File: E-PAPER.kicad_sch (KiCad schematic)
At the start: 33 parts, among them J6 Conn_01x34_Female, J7 Conn_01x40_Female, U10 TPS65185RGZR

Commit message: Update (Display)
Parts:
- removed C83: 4µ7, Capacitor_SMD:C_0805_2012Metric, symbol Device:C
- removed R50: R, symbol Device:R
- added C85: 22µ, Capacitor_SMD:C_0603_1608Metric, symbol Device:C
- added R54: 1MEG, symbol Device:R
- C84: value C -> 22µ; footprint (none) -> Capacitor_SMD:C_0603_1608Metric; LCSC (none) -> C2762594
- L4: value 4µ7 -> 2µ2; footprint (none) -> Inductor_SMD:L_1008_2520Metric; LCSC (none) -> C315713
- L5: footprint (none) -> Inductor_SMD:L_1008_2520Metric; LCSC (none) -> C379997
- R55: renamed from R51; value R -> 47K5; LCSC (none) -> C2930010
- R56: renamed from R52; value R -> 1MEG; LCSC (none) -> C2909328
- R57: renamed from R53; value R -> 52K3; LCSC (none) -> C321542
- renumbered C74 to C75, C75 to C76, C76 to C77, C77 to C78, C78 to C79, C79 to C80, C80 to C81, C81 to C82, C82 to C83, C85 to C86, C86 to C87, C87 to C88, C88 to C89, C89 to C90, C90 to C91, C91 to C92
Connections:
- net AGND2: now also J6.26 (Pin_26), J6.3 (Pin_3), J6.32 (Pin_32), J6.7 (Pin_7), J6.9 (Pin_9), J7.12 (Pin_12), J7.22 (Pin_22), J7.9 (Pin_9), C85.2
- net VB: now also J6.33 (Pin_33), J7.36 (Pin_36)
- net VDDH: now also J6.34 (Pin_34), J7.3 (Pin_3), R54.1
- net VDD_FB: now also R54.2
- net VEE: now also J6.2 (Pin_2), J7.1 (Pin_1)
- net VN: now also J6.1 (Pin_1), J7.38 (Pin_38)
- net XLE: now reaches J6.10 (Pin_10)
- net XLE: now also J7.32 (Pin_32)
- net XOE: now reaches J6.11 (Pin_11)
- net XOE: now also J7.33 (Pin_33)
- net XSTL: now reaches J6.12 (Pin_12)
- net XSTL: now also J7.31 (Pin_31)
- net XD0: now reaches J6.13 (Pin_13), J7.14 (Pin_14)
- net XD1: now reaches J6.14 (Pin_14), J7.15 (Pin_15)
- net XD2: now reaches J6.15 (Pin_15), J7.16 (Pin_16)
- net XD3: now reaches J6.16 (Pin_16), J7.17 (Pin_17)
- net XD4: now reaches J6.17 (Pin_17), J7.18 (Pin_18)
- net XD5: now reaches J6.18 (Pin_18), J7.19 (Pin_19)
- net XD6: now reaches J6.19 (Pin_19), J7.20 (Pin_20)
- net XD7: now reaches J6.20 (Pin_20), J7.21 (Pin_21)
- net VCOM: now reaches J6.21 (Pin_21)
- net VCOM: now also C84.1, J7.10 (Pin_10), U10.15 (VCOM)
- net XMODE: now reaches J6.27 (Pin_27)
- net XMODE: now also J7.6 (Pin_6)
- net XCKV: now reaches J6.28 (Pin_28)
- net XCKV: now also J7.7 (Pin_7)
- net XSPV: now reaches J6.29 (Pin_29)
- net XSPV: now also J7.8 (Pin_8)
- net XBORDER: now reaches J6.31 (Pin_31)
- net XBORDER: now also J7.40 (Pin_40)
- net VDD: now reaches J6.6 (Pin_6), J7.5 (Pin_5)
- net VDD: now also J7.11 (Pin_11), J7.34 (Pin_34), U10.46 (V3P3)
- net XCLK: now reaches J6.8 (Pin_8), J7.13 (Pin_13)
- net at U10.1 (VREF): now also C85.1; no longer C84.1
- net XVCOM_CTRL: now reaches U10.12 (VCOM_CTRL)
- net XSCL: now reaches U10.17 (SCL)
- net XSDA: now reaches U10.18 (SDA)
- net X~{INT}: now reaches U10.2 (~{INT})
- net XPWRUP: now reaches U10.21 (PWRUP)
- net XPWR_GOOD: now reaches U10.23 (PWR_GOOD)
- net XWAKEU: now reaches U10.5 (WAKEUP)
- net XD8: now reaches J7.23 (Pin_23)
- net XD9: now reaches J7.24 (Pin_24)
- net XD10: now reaches J7.25 (Pin_25)
- net XD11: now reaches J7.26 (Pin_26)
- net XD12: now reaches J7.27 (Pin_27)
- net XD13: now reaches J7.28 (Pin_28)
- net XD14: now reaches J7.29 (Pin_29)
- net XD15: now reaches J7.30 (Pin_30)
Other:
- moved on the sheet: C83, C86, C88, R56, R57, U10

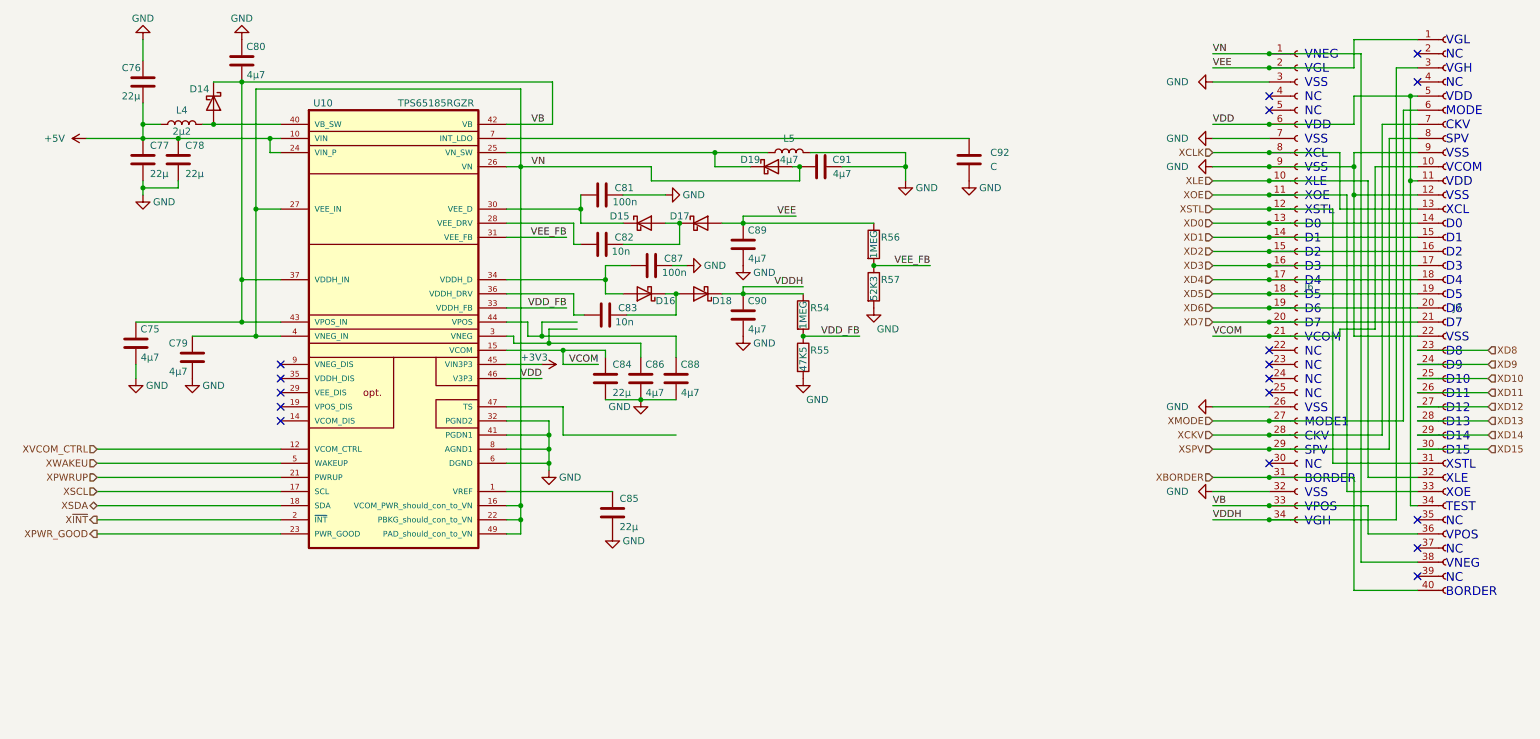
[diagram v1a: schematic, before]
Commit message: Add Audio
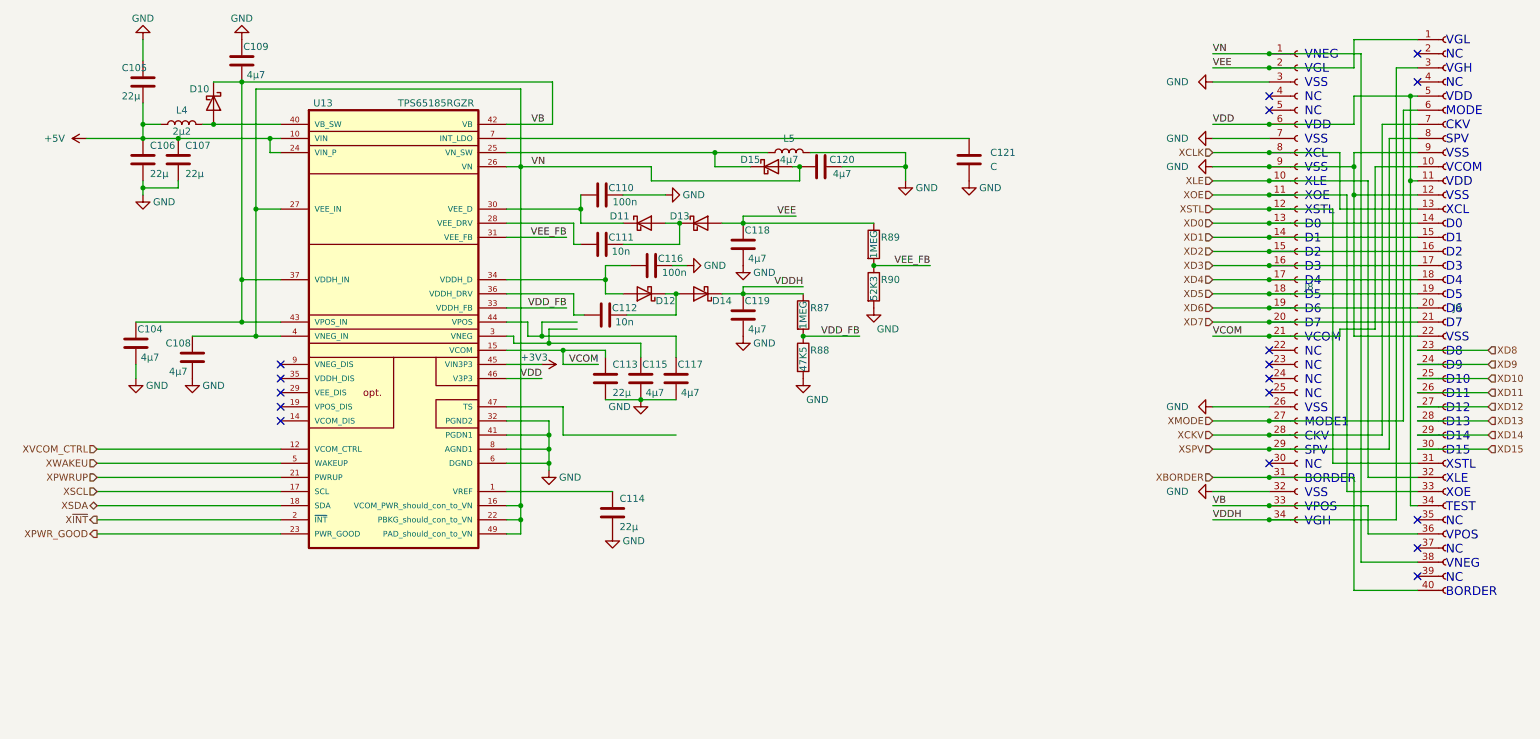
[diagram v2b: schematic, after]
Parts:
- renumbered C75 to C104, C76 to C105, C77 to C106, C78 to C107, C79 to C108, C80 to C109, C81 to C110, C82 to C111, C83 to C112, C84 to C113, C85 to C114, C86 to C115, C87 to C116, C88 to C117, C89 to C118, C90 to C119, C91 to C120, C92 to C121, D14 to D10, D15 to D11, D16 to D12, D17 to D13, D18 to D14, D19 to D15, J6 to J8, J7 to J9, R54 to R87, R55 to R88, R56 to R89, R57 to R90, U10 to U13

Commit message: Display Update
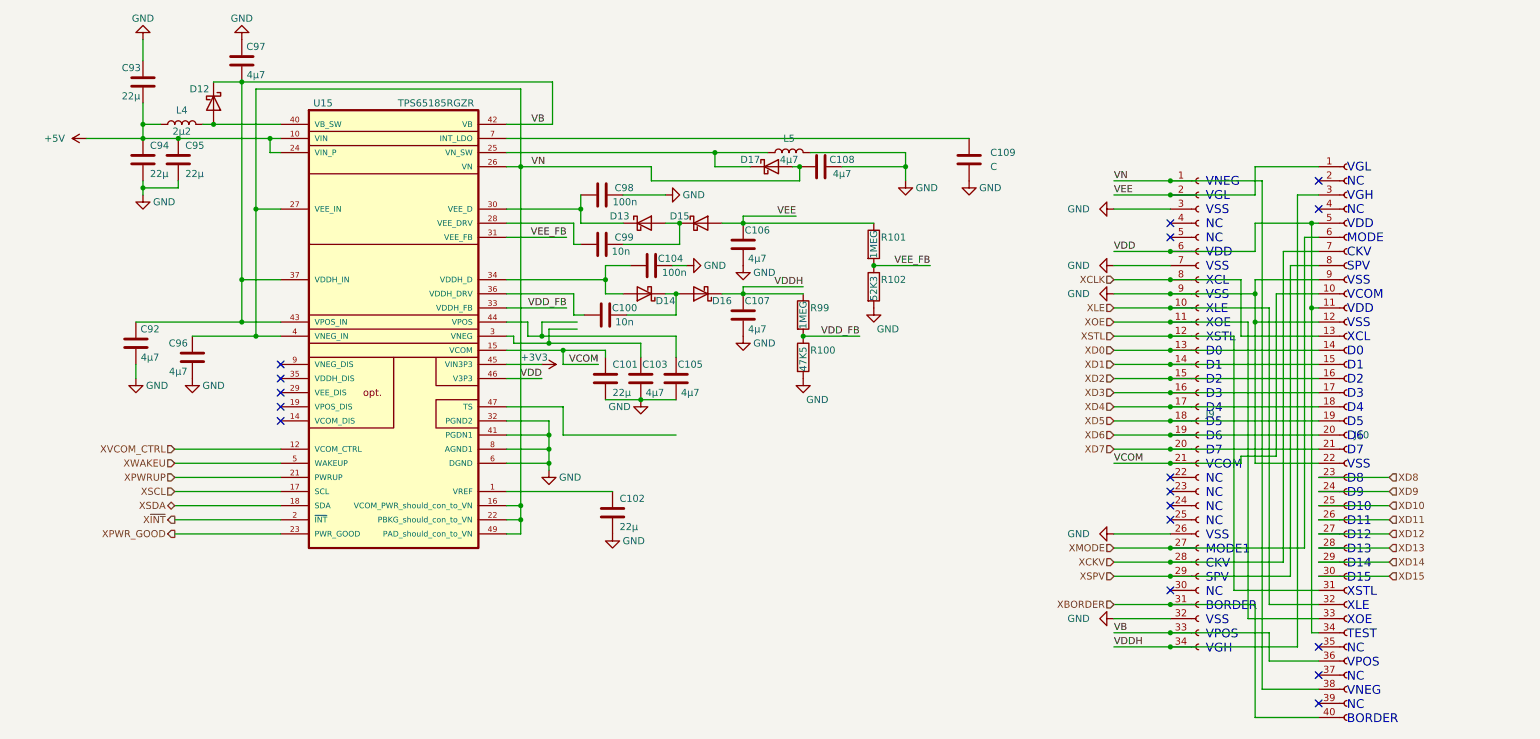
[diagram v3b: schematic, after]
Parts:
- renumbered C112 to C100, C113 to C101, C114 to C102, C115 to C103, C116 to C104, C117 to C105, C118 to C106, C119 to C107, C120 to C108, C121 to C109, C104 to C92, C105 to C93, C106 to C94, C107 to C95, C108 to C96, C109 to C97, C110 to C98, C111 to C99, D10 to D12, D11 to D13, D12 to D14, D13 to D15, D14 to D16, D15 to D17, J9 to J10, J8 to J9, R88 to R100, R89 to R101, R90 to R102, R87 to R99, U13 to U15
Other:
- moved on the sheet: J10, J9

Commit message: update DDR
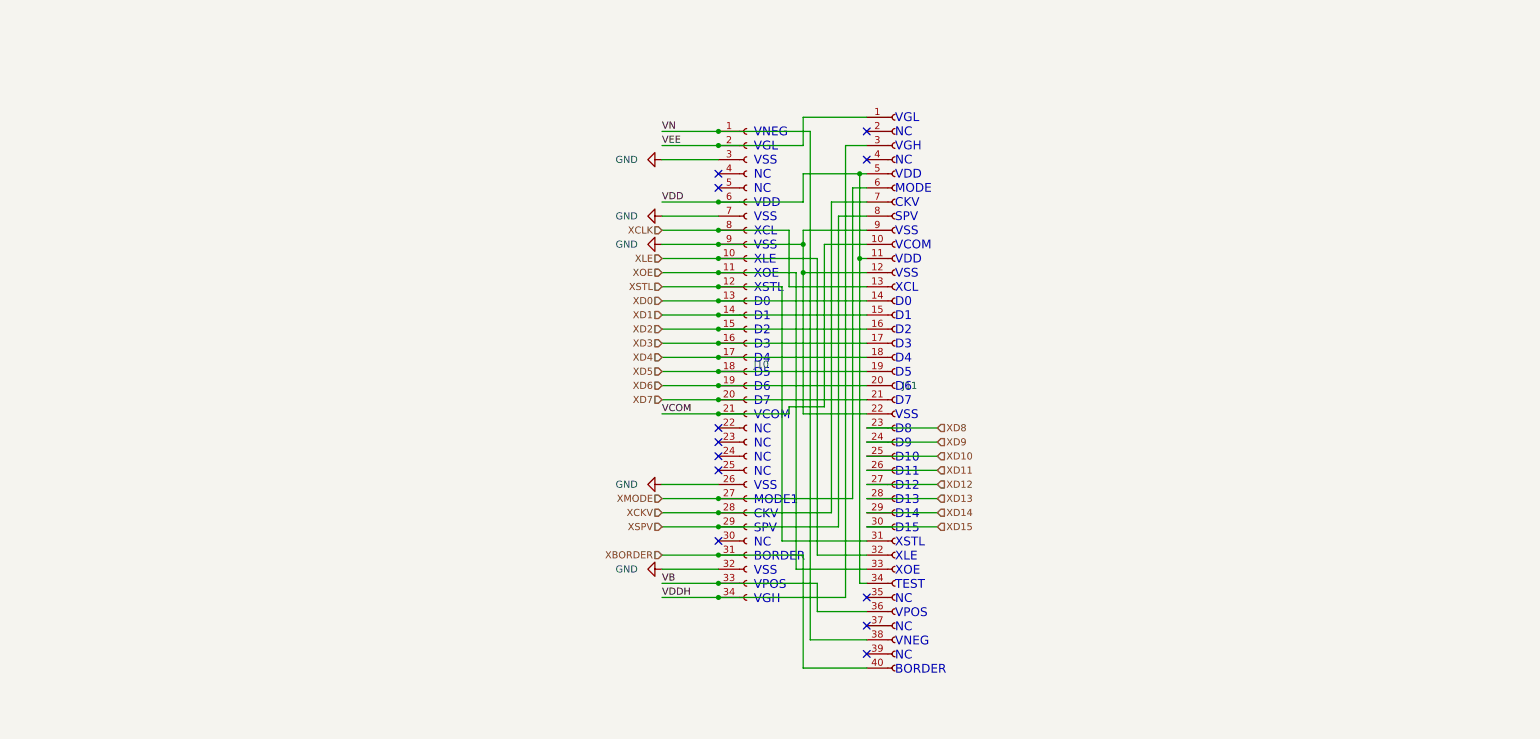
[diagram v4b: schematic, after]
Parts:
- removed C100, C99: 10n, Capacitor_SMD:C_0402_1005Metric, symbol Device:C
- removed C101, C102, C93, C94, C95: 22µ, Capacitor_SMD:C_0603_1608Metric, symbol Device:C
- removed C103, C105, C106, C107, C108, C92, C96, C97: 4µ7, Capacitor_SMD:C_0805_2012Metric, symbol Device:C
- removed C104, C98: 100n, Capacitor_SMD:C_0402_1005Metric, symbol Device:C
- removed C109: C, symbol Device:C
- removed D12, D13, D14, D15, D16, D17: D_Schottky, TheBrutzlers_Lib:SOD-123FL, symbol Device:D_Schottky
- removed L4: 2µ2, Inductor_SMD:L_1008_2520Metric, symbol Device:L
- removed L5: 4µ7, Inductor_SMD:L_1008_2520Metric, symbol Device:L
- removed R100: 47K5, symbol Device:R
- removed R101, R99: 1MEG, symbol Device:R
- removed R102: 52K3, symbol Device:R
- removed U15: TPS65185RGZR, QFN50P700X700X100-49N, symbol TheBrutzlers_Lib:TPS65185RGZR
- renumbered J9 to J10, J10 to J11
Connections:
- net AGND2 renamed GND
- no-connect marks 17 -> 12
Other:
- moved on the sheet: J10, J11
